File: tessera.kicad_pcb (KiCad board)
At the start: 4 copper layers, 54 x 85.6 mm, 108 parts, among them J1 USB-C, J2 532610271, J3 PinHeader_2x05, Q1 NTK3139P, Q2 NTK3134N, Q3 NTK3134N, SW1 EVQP7A01P, SW2 EVQP7A01P, U1 USBLC6-2P6, U2 BQ25170J, U3 TPS62840DLCR, U4 ISP1807-LR-RS, U5 D3V3XA4B10LP, U6 ST25DV64KC-JF6D3, U7 STSAFA120DFSPL05

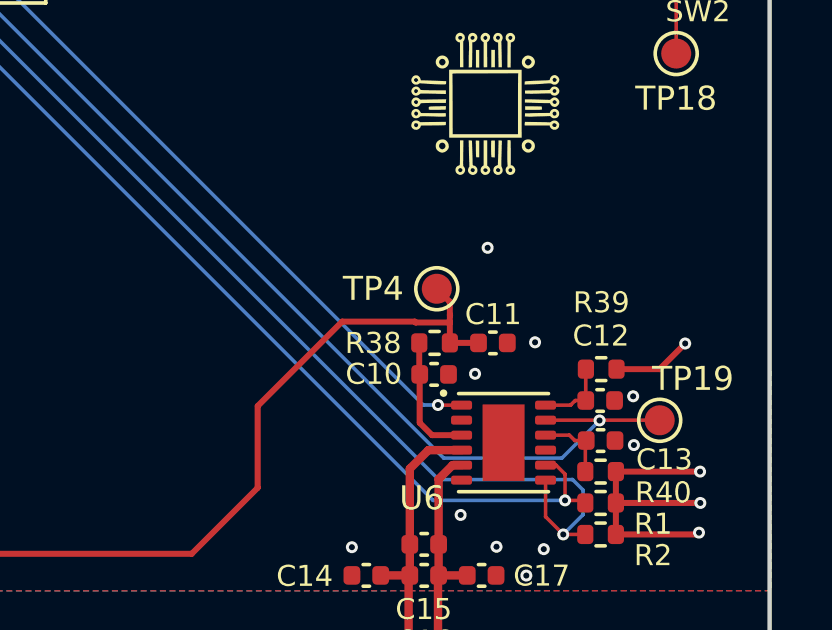
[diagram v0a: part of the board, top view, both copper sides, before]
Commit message: fix(hardware): resolve KiBot iBoM crash and stale symbol warning
- Add G1-G5 Workart artwork as schematic symbols marked exclude-from-BOM,
  instead of PCB-only footprints.
- Works around a KiBot iBoM crash caused by PCB-only footprints having
  no parent sheet in the variant netlist  (upstream: INTI-CMNB/KiBot#955)
- Register the Workart.kicad_sym library in sym-lib-table
- Bump lib submodule to add the matching Workart schematic symbols
- Fix W043 warning: remove stale lib_name override for J2 in
  power.kicad_sch
- CI: checkout submodules recursively and regenerate catalog.sqlite
  from lib_db/source/*.csv (lib/lib_db/build_db.py) so the "catalog"
  database library resolves during CI runs
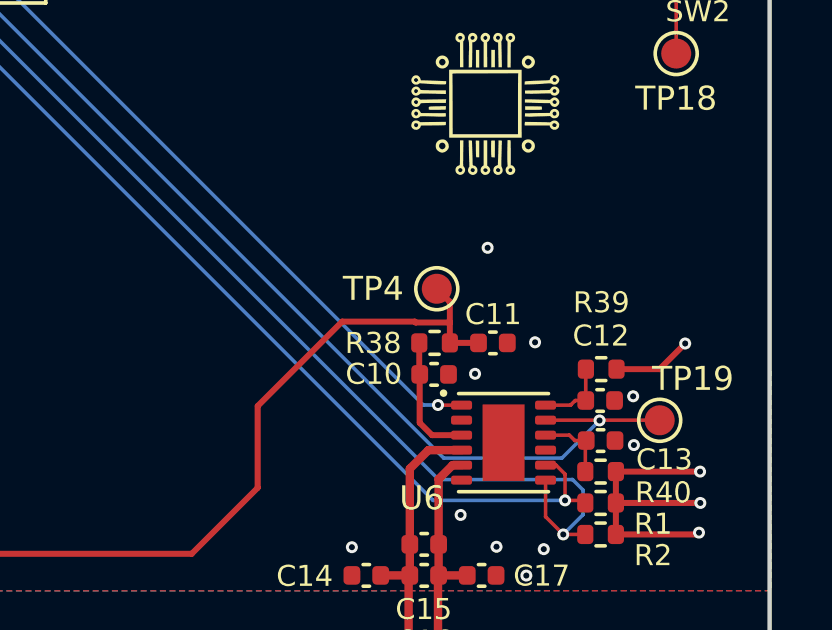
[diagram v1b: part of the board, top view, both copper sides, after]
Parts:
- G1: value LOGO -> WA_APS_Logo
- G2: value LOGO -> WA_tessera_Name
- G3: value LOGO -> WA_tessera_light_bulb
- G4: value LOGO -> WA_tessera_linkedin_qr
- G5: value LOGO -> WA_tessera_binary
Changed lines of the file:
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@@
 			)
 		)
-		(property "Value" "LOGO"
+		(property "Value" "WA_APS_Logo"
 			(at -0.03 4.06 0)
 			(layer "F.SilkS")
@@
 			)
 		)
+		(property "Revision" "01"
+			(at 0 0 0)
+			(unlocked yes)
+			(layer "F.Fab")
+			(hide yes)
+			(effects
+				(font
+					(size 1 1)
+					(thickness 0.15)
+				)
+			)
+		)
+		(sheetname "Project Architecture")
+		(sheetfile "Project Architecture.kicad_sch")
 		(attr board_only exclude_from_pos_files exclude_from_bom)
 		(fp_poly
@@
 			)
 		)
-		(property "Value" "LOGO"
+		(property "Value" "WA_tessera_Name"
 			(at 0.75 0 0)
 			(layer "B.SilkS")
@@
 			)
 		)
+		(property "Revision" "01"
+			(at 0 0 180)
+			(unlocked yes)
+			(layer "B.Fab")
+			(hide yes)
+			(effects
+				(font
+					(size 1 1)
+					(thickness 0.15)
+				)
+				(justify mirror)
+			)
+		)
+		(sheetname "Project Architecture")
+		(sheetfile "Project Architecture.kicad_sch")
 		(attr board_only exclude_from_pos_files exclude_from_bom)
 		(fp_poly
@@
 			)
 		)
-		(property "Value" "LOGO"
+		(property "Value" "WA_tessera_linkedin_qr"
 			(at 0.75 0 0)
 			(layer "B.SilkS")
@@
 			)
 		)
+		(property "Revision" "01"
+			(at 0 0 180)
+			(unlocked yes)
+			(layer "B.Fab")
+			(hide yes)
+			(effects
+				(font
+					(size 1 1)
+					(thickness 0.15)
+				)
+				(justify mirror)
+			)
+		)
+		(sheetname "Project Architecture")
+		(sheetfile "Project Architecture.kicad_sch")
 		(attr board_only exclude_from_pos_files exclude_from_bom)
 		(fp_poly
@@
 			)
 		)
-		(property "Value" "LOGO"
+		(property "Value" "WA_tessera_light_bulb"
 			(at 0.75 0 0)
 			(layer "B.SilkS")
@@
 			)
 		)
+		(property "Revision" "01"
+			(at 0 0 180)
+			(unlocked yes)
+			(layer "B.Fab")
+			(hide yes)
+			(effects
+				(font
+					(size 1 1)
+					(thickness 0.15)
+				)
+				(justify mirror)
+			)
+		)
+		(sheetname "Project Architecture")
+		(sheetfile "Project Architecture.kicad_sch")
 		(attr board_only exclude_from_pos_files exclude_from_bom)
 		(fp_poly
@@
 			)
 		)
-		(property "Value" "LOGO"
+		(property "Value" "WA_tessera_binary"
 			(at 0.75 0 0)
 			(layer "B.SilkS")
@@
 			)
 		)
+		(property "Revision" "01"
+			(at 0 0 180)
+			(unlocked yes)
+			(layer "B.Fab")
+			(hide yes)
+			(effects
+				(font
+					(size 1 1)
+					(thickness 0.15)
+				)
+				(justify mirror)
+			)
+		)
+		(sheetname "Project Architecture")
+		(sheetfile "Project Architecture.kicad_sch")
 		(attr board_only exclude_from_pos_files exclude_from_bom)
 		(fp_poly
@@
 	)
 	(gr_line
-		(start 176.915 68.34)
+		(start 176.78 68.34)
 		(end 175.96 68.34)
 		(stroke
@@
 	)
 	(gr_line
-		(start 176.995 71.905)
+		(start 176.78 72.015)
 		(end 173.595 73.765)
 		(stroke
@@
 	)
 	(gr_line
-		(start 176.905 69.44)
+		(start 176.785 69.44)
 		(end 176.56 69.44)
 		(stroke
@@
 	)
 	(gr_line
-		(start 176.965 67.34)
+		(start 176.785 67.34)
 		(end 175.56 67.34)
 		(stroke
@@
 	)
 	(gr_line
-		(start 176.955 70.575)
-		(end 168.66 75.24)
+		(start 176.78 70.645)
+		(end 168.485 75.31)
 		(stroke
 			(width 0.25)
@@
 	)
 	(gr_line
-		(start 176.925 65.64)
+		(start 176.785 65.64)
 		(end 176.66 65.64)
 		(stroke
@@
 		(width 0.2)
 		(layer "F.Cu")
-		(net 12)
-	)
-	(segment
-		(start 166.340004 73.875)
-		(end 166.33 73.864996)
-		(width 0.2)
-		(layer "F.Cu")

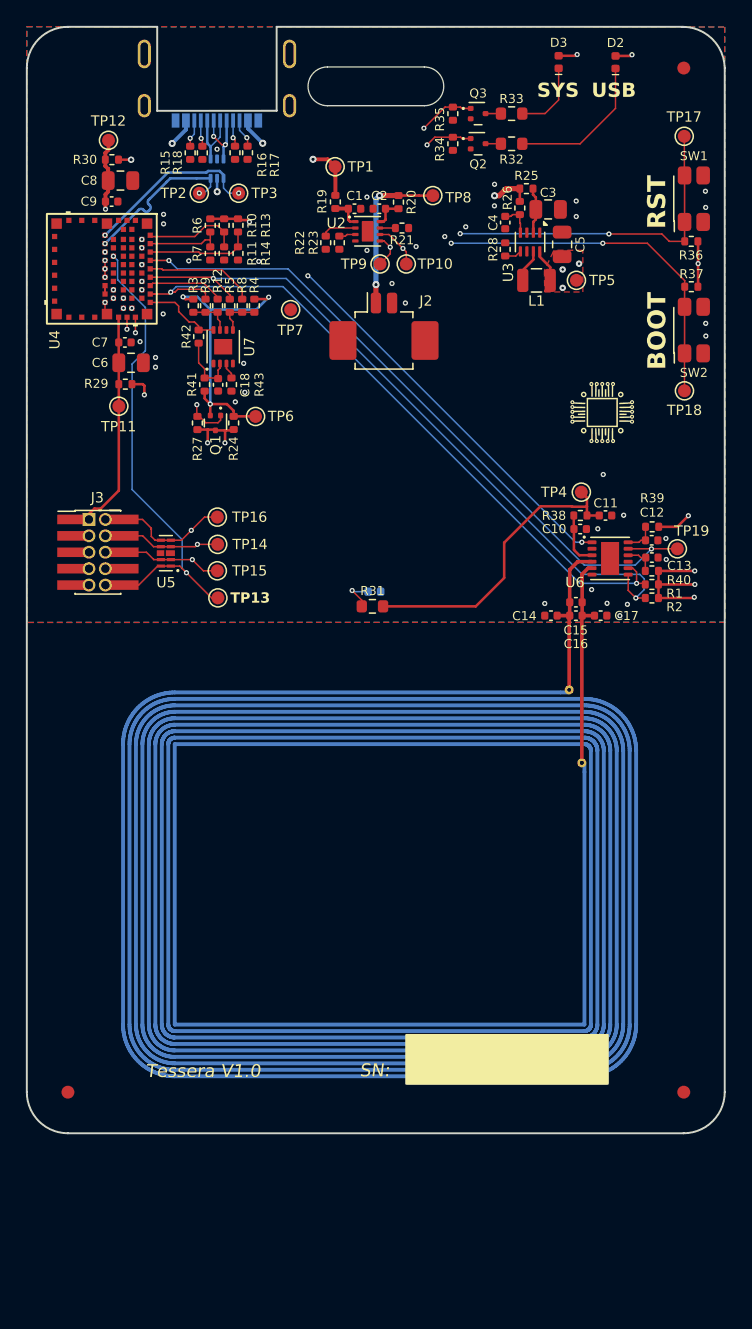
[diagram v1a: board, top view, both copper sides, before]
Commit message: feat(hardware): add board logo, per-side assembly tables
- Bump lib submodule: fix mismatched drill diameters on the two
  THT pads of the NFC_40x30_N9_ST_ST25DV footprint
- Embed the APS logo image on every schematic sheet's title block
- Move the impedance-controlled differential pair from L1/L2 to
  L4/L3 and update its target to 90 Ω in the impedance table
- KiBot: add per-side (top/bottom) CSV position tables and wire them
  into the assembly PDF as pick & place tables
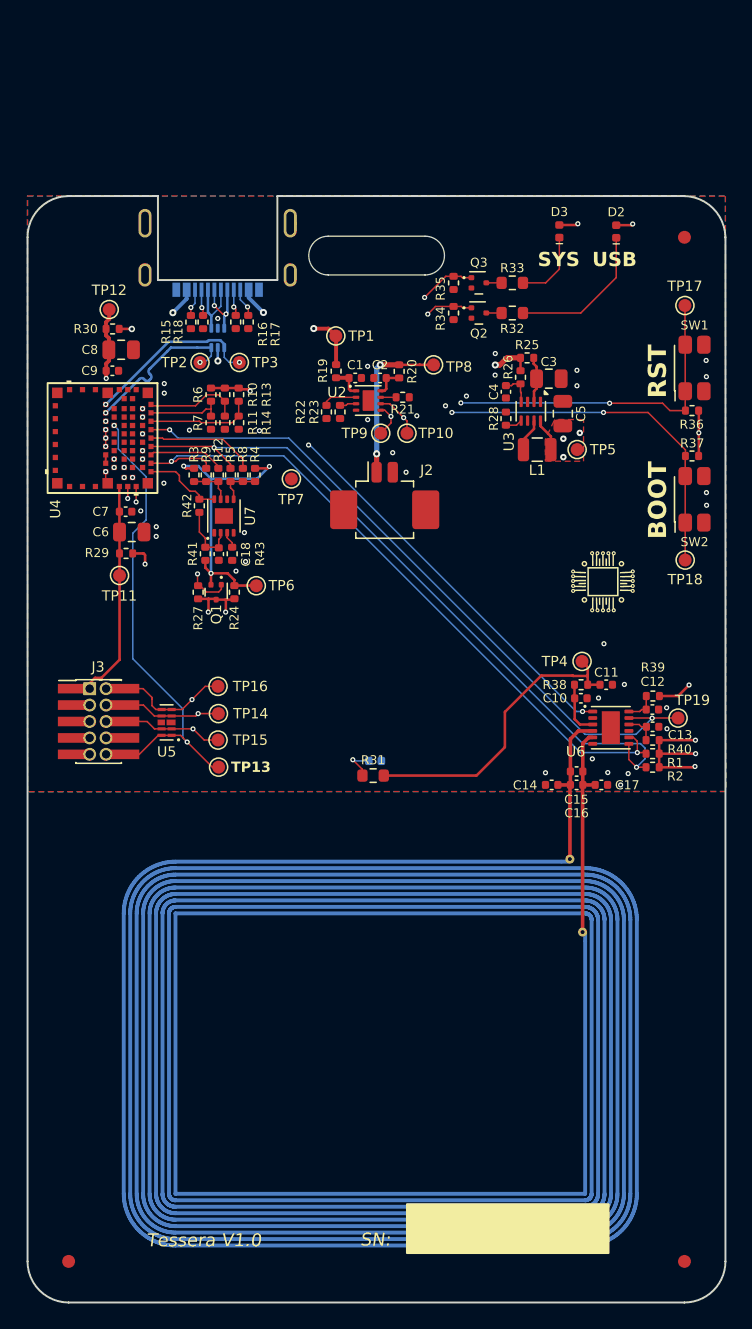
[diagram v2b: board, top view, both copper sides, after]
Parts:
- moved D1 13.1 mm to (149.9, 93.8)
- moved G1 13.1 mm to (167.6, 79.9)
- moved C3 13.1 mm to (163.4, 64.2)
- moved C4 13.1 mm to (160.1, 65.2)
- moved C6 13.1 mm to (131.1, 76.1)
- moved D2 13.1 mm to (168.6, 52.8)
- moved J2 13.1 mm to (150.7, 73.9)
- moved Q2 13.1 mm to (158.0, 59.1)
- moved R10 13.1 mm to (138.3, 65.5)
- moved R11 13.1 mm to (138.3, 67.6)
- moved R12 13.1 mm to (137.8, 71.7)
- moved R13 13.1 mm to (139.4, 65.5)
- moved R14 13.1 mm to (139.4, 67.6)
- moved R22 13.1 mm to (146.2, 66.8)
- moved R23 13.1 mm to (147.2, 66.8)
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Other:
- board text removed: "30°"
- board text removed: "3× 120°"
